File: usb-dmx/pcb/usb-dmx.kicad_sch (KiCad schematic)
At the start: 21 parts, among them J1 USB_C_Receptacle_USB2.0_16P, J2 USB_A, SW1 PTS526_SM15_SMTR2_LFS, U1 IP4234CZ6, U2 ADP2108AUJ-3.3, U3 ESP32-S3-MINI-1U, U4 ST485E

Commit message: adding external antenna to schematic
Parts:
- added AE1: Antenna, symbol Device:Antenna
- added J3: Conn_01x01_Pin, symbol Connector:Conn_01x01_Pin
- added J4: Conn_01x01_Socket, symbol Connector:Conn_01x01_Socket
- D1: DESCRIPTION (none) -> Only Order 1 per 10 LEDs
- SW1: DESCRIPTION Tactile Switches 50mA 12VDC, 5.2x5.2mm, 1.5mm H, 160gf, G l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 -> (none)
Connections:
- new net: AE1.1 (A), J4.1 (Pin_1)
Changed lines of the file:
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@@
+	)
+	(symbol
+		(lib_id "Connector:Conn_01x01_Socket")
+		(at 388.62 66.04 270)
+		(unit 1)
+		(exclude_from_sim no)
+		(in_bom no)
+		(on_board no)
+		(dnp no)
+		(property "Reference" "J4"
+			(at 390.144 61.722 90)
+			(effects
+				(font
+					(size 1.27 1.27)
+				)
+				(justify left)
+			)
+		)
+		(property "Value" "Conn_01x01_Socket"
+			(at 390.144 64.77 90)
+			(effects
+				(font
+					(size 1.27 1.27)
+				)
+				(justify left)
+			)
+		)
+		(property "Footprint" ""
+			(at 388.62 66.04 0)
+			(effects
+				(font
+					(size 1.27 1.27)
+				)
+				(hide yes)
+			)
+		)
+		(property "Datasheet" "~"
+			(at 388.62 66.04 0)
+			(effects
+				(font
+					(size 1.27 1.27)
+				)
+				(hide yes)
+			)
+		)
+		(property "Description" "Generic connector, single row, 01x01, script generated"
+			(at 388.62 66.04 0)
+			(effects
+				(font
+					(size 1.27 1.27)
+				)
+				(hide yes)
+			)
+		)
+		(pin "1"
+		)
+		(instances
+			(project ""
+				(path "/8846f2fa-8392-4ca0-b0ea-63a42c0612b6"
+					(reference "J4")
+					(unit 1)
+				)
+			)
+		)
+	)
+	(symbol
+		(lib_id "Device:Antenna")
+		(at 388.62 55.88 0)
+		(unit 1)
+		(exclude_from_sim no)
+		(in_bom yes)
+		(on_board no)
+		(dnp no)
+		(property "Reference" "AE1"
+			(at 391.16 55.2449 0)
+			(effects
+				(font
+					(size 1.27 1.27)
+				)
+				(justify left)
+			)
+		)
+		(property "Value" "Antenna"
+			(at 391.16 57.7849 0)
+			(effects
+				(font
+					(size 1.27 1.27)
+				)
+				(justify left)
+			)
+		)
+		(property "Footprint" ""
+			(at 388.62 55.88 0)
+			(effects
+				(font
+					(size 1.27 1.27)
+				)
+				(hide yes)
+			)
+		)
+		(property "Datasheet" "~"
+			(at 388.62 55.88 0)
+			(effects
+				(font
+					(size 1.27 1.27)
+				)
+				(hide yes)
+			)
+		)
+		(property "Description" "Antenna"
+			(at 388.62 55.88 0)
+			(effects
+				(font
+					(size 1.27 1.27)
+				)
+				(hide yes)
+			)
+		)
+		(property "MOUSER_PART_NUMBER" "538-214415-0011"
+			(at 401.32 53.34 0)
+			(effects
+				(font
+					(size 1.27 1.27)
+				)
+			)
+		)
+		(pin "1"
+		)
+		(instances
+			(project ""
+				(path "/8846f2fa-8392-4ca0-b0ea-63a42c0612b6"
+					(reference "AE1")
+					(unit 1)
+				)
+			)
+		)
 	)
 	(symbol
@@
 	)
 	(symbol
+		(lib_id "Connector:Conn_01x01_Pin")
+		(at 388.62 66.04 270)
+		(unit 1)
+		(exclude_from_sim no)
+		(in_bom yes)
+		(on_board no)
+		(dnp no)
+		(property "Reference" "J3"
+			(at 390.144 67.564 90)
+			(effects
+				(font
+					(size 1.27 1.27)
+				)
+				(justify left)
+			)
+		)
+		(property "Value" "Conn_01x01_Pin"
+			(at 390.144 69.85 90)
+			(effects
+				(font
+					(size 1.27 1.27)
+				)
+				(justify left)
+			)
+		)
+		(property "Footprint" ""
+			(at 388.62 66.04 0)
+			(effects
+				(font
+					(size 1.27 1.27)
+				)
+				(hide yes)
+			)
+		)
+		(property "Datasheet" "~"
+			(at 388.62 66.04 0)
+			(effects
+				(font
+					(size 1.27 1.27)
+				)
+				(hide yes)
+			)
+		)
+		(property "Description" "Generic connector, single row, 01x01, script generated"
+			(at 388.62 66.04 0)
+			(effects
+				(font
+					(size 1.27 1.27)
+				)
+				(hide yes)
+			)
+		)
+		(property "MOUSER_PART_NUMBER" "485-5444"
+			(at 393.954 78.232 0)
+			(effects
+				(font
+					(size 1.27 1.27)
+				)
+			)
+		)
+		(pin "1"
+		)
+		(instances
+			(project ""
+				(path "/8846f2fa-8392-4ca0-b0ea-63a42c0612b6"
+					(reference "J3")
+					(unit 1)
+				)
+			)
+		)
+	)
+	(symbol
 		(lib_id "power:GND")
 		(at 248.92 87.63 0)
@@
 			)
 		)
-		(property "DESCRIPTION" "Tactile Switches 50mA 12VDC, 5.2x5.2mm, 1.5mm H, 160gf, G leads, No ground pin, metal actuator"
+		(property "DESCRIPTION" ""
 			(at 123.19 195.58 0)
 			(effects
@@
 			(at 73.66 195.58 0)
 			(effects
+				(font
+					(size 1.27 1.27)
+				)
+			)
+		)
+		(property "DESCRIPTION" "Only Order 1 per 10 LEDs"
+			(at 73.66 195.58 0)
+			(effects

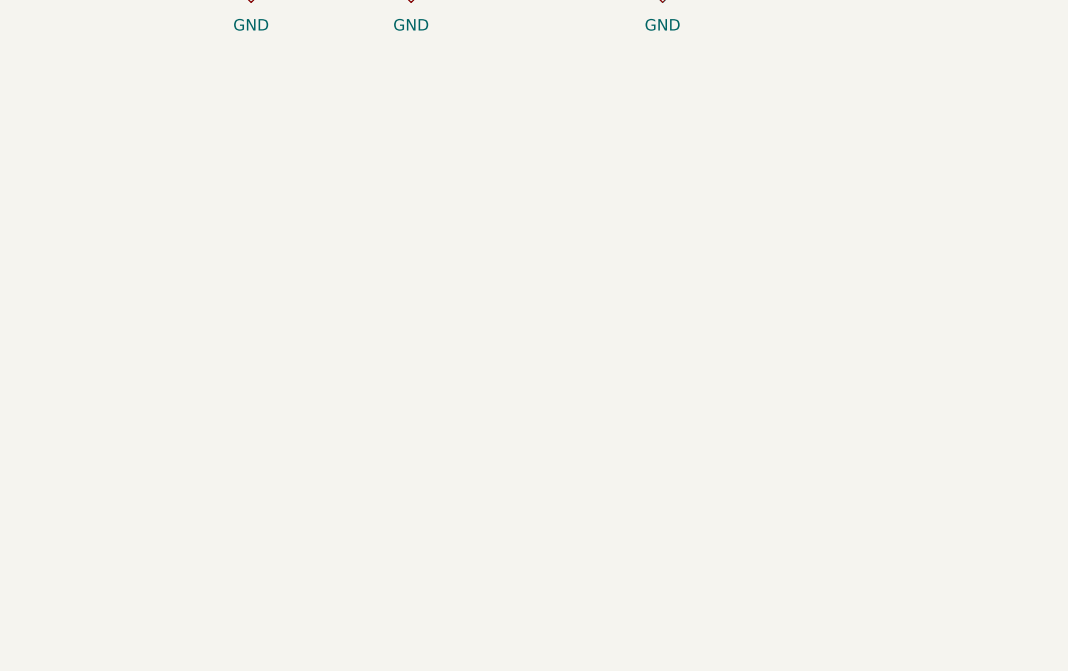
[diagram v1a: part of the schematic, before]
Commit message: Adding other Voltage Regulator
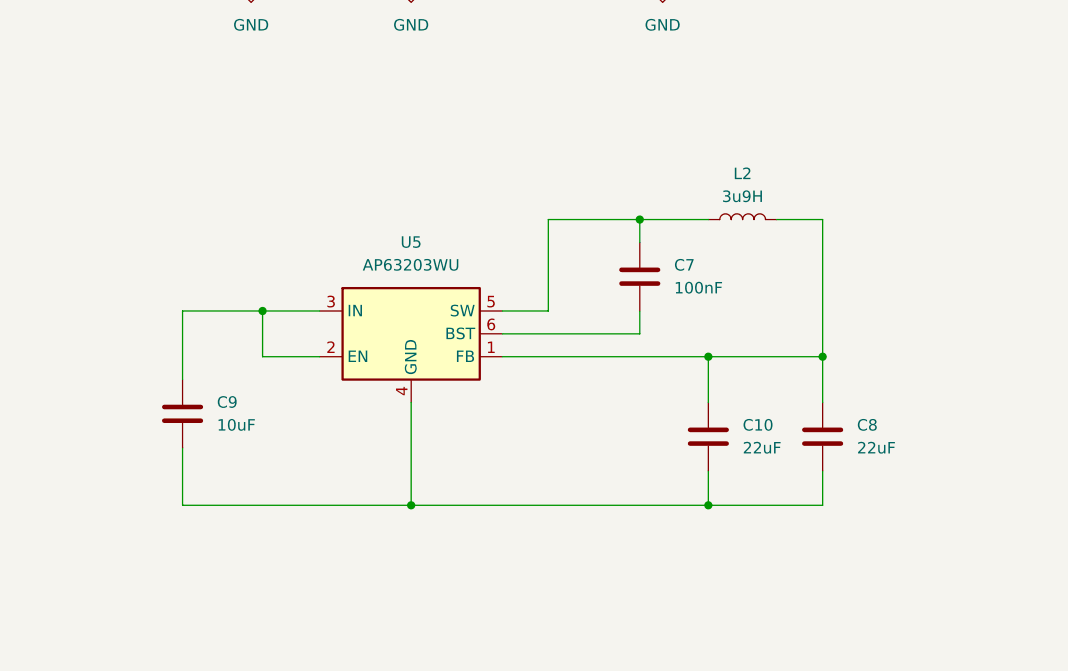
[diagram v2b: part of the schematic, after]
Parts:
- added C10, C8: 22uF, Capacitor_SMD:C_0805_2012Metric, symbol Device:C
- added C7: 100nF, Capacitor_SMD:C_0805_2012Metric, symbol Device:C
- added C9: 10uF, Capacitor_SMD:C_0805_2012Metric, symbol Device:C
- added L2: 3u9H, Inductor_SMD:L_0805_2012Metric, symbol Device:L
- added U5: AP63203WU, Package_TO_SOT_SMD:TSOT-23-6, symbol Regulator_Switching:AP63203WU
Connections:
- new net: C10.1, C8.1, L2.2, U5.1 (FB)
- new net: C10.2, C8.2, C9.2, U5.4 (GND)
- new net: C7.1, L2.1, U5.5 (SW)
- new net: C7.2, U5.6 (BST)
- new net: C9.1, U5.2 (EN), U5.3 (IN)
